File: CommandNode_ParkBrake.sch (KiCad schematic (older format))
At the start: 0 parts

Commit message: Created isolated RS585 interfaces and completed park brake.
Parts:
- added D? (x2): BAS16,215, RLOOP_FOOTPRINTS:rLoop_SOT23, symbol BAS16,215
- added P? (x2): TE_640456-8, RLOOP_FOOTPRINTS:rLoop_TE640456-8, symbol TE_640456-8
- added RL? (x2): TQ2-5V, RLOOP_FOOTPRINTS:rLoop_DIP10, symbol TQ2-5V
- added U? (x2): NUD3124LT1G, RLOOP_FOOTPRINTS:rLoop_SOT23, symbol NUD3124LT1G
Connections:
- net labels added: +24V_A, +5V_A, GNDD, PARK_BRAKE
- wire segments 0 -> 27
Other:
- note added: "Solenoids are 0.4A"
- note added: "rLoop - Command Node\nPark Brake Interface"

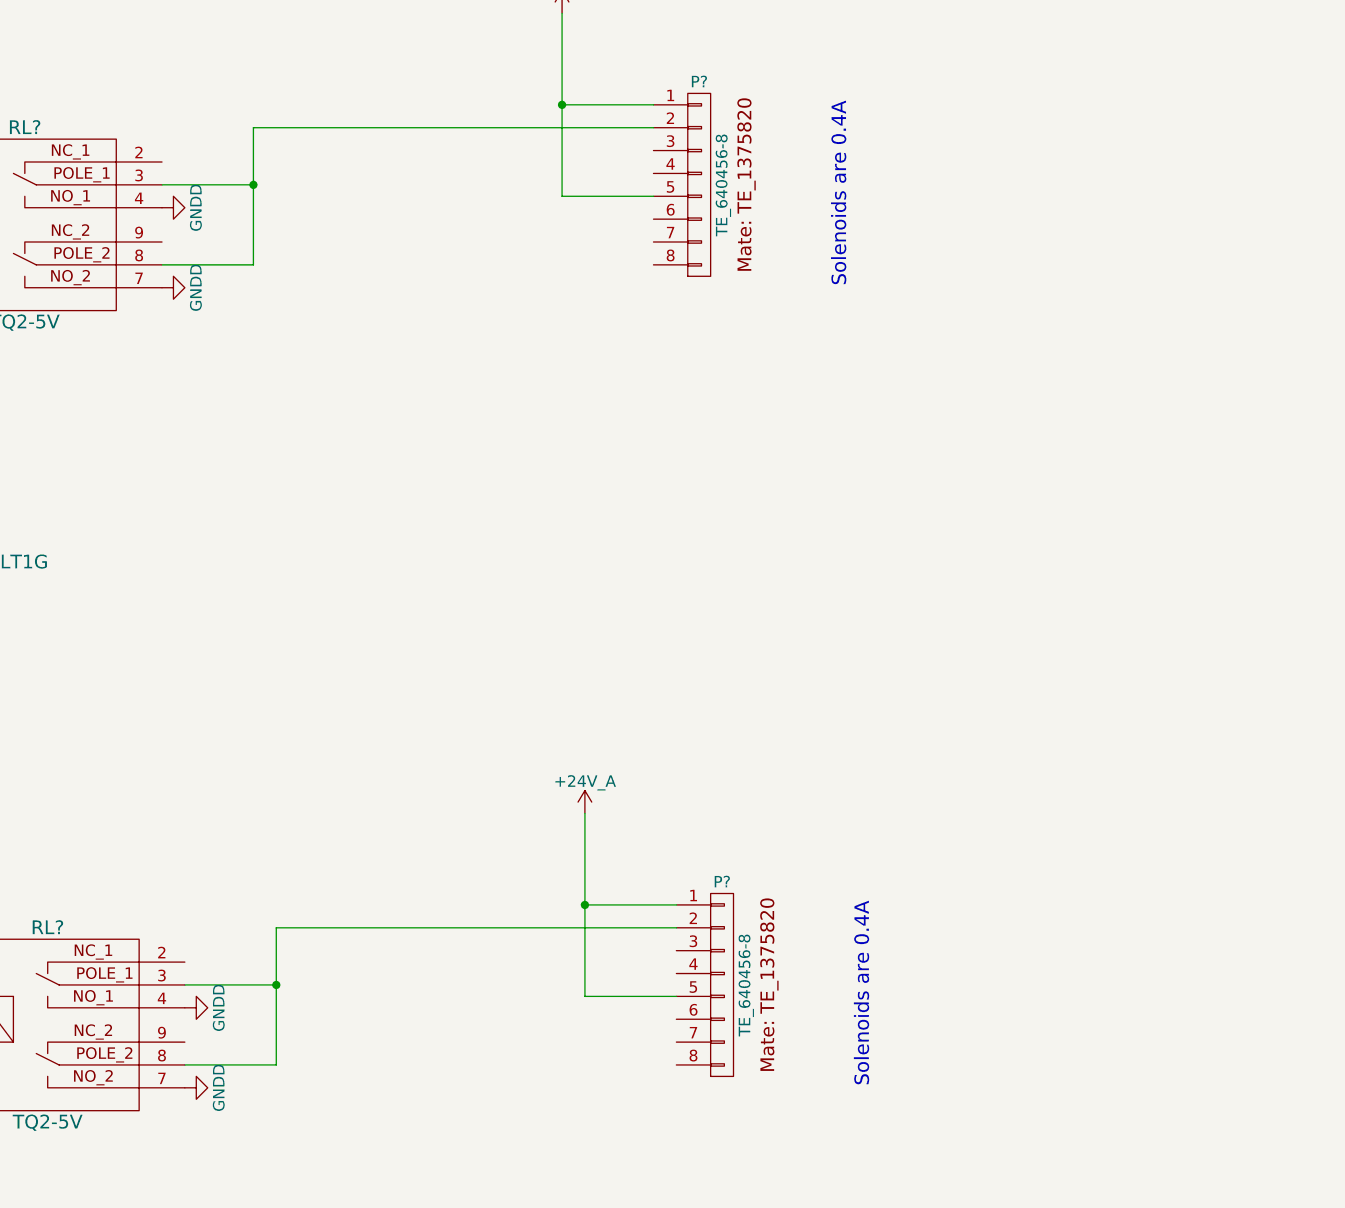
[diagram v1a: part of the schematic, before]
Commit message: Finish and print schematics for review
Lifting mechanism, charger interface, Data Enable on HE controller
RS585, Park Brake and node core.
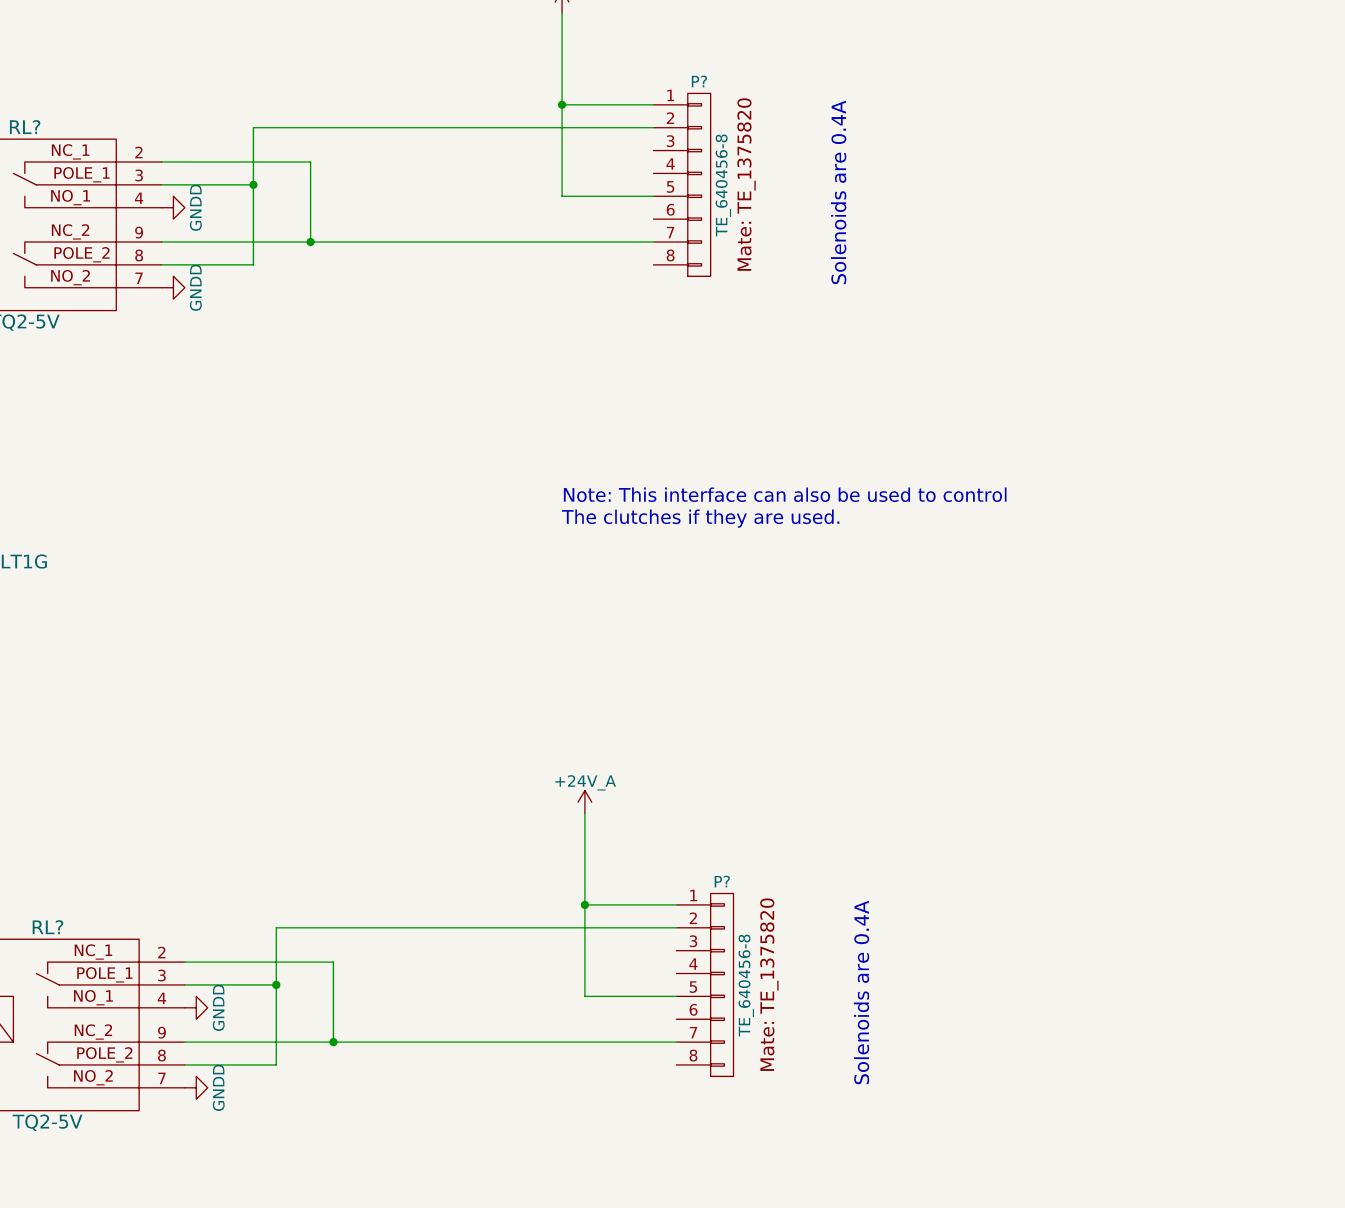
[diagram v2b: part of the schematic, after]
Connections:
- wire segments 27 -> 33
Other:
- note added: "Note: This interface can also be used to control \nThe clutches if they are used."
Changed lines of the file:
@@
 $Descr A3 16535 11693
 encoding utf-8
-Sheet 2 7
+Sheet 2 8
 Title "Park Brake Interface"
 Date ""
@@
 	5000 8650 5000 5150
 Connection ~ 5000 5150
+Text Notes 9550 5350 0    60   ~ 0
+Note: This interface can also be used to control \nThe clutches if they are used.
+Wire Wire Line
+	7800 4100 9950 4100
+Wire Wire Line
+	7800 3750 8450 3750
+Wire Wire Line
+	8450 3750 8450 4100
+Connection ~ 8450 4100
+Wire Wire Line
+	7900 7600 10050 7600
+Wire Wire Line
+	8550 7250 8550 7600
+Connection ~ 8550 7600
+Wire Wire Line
+	7900 7250 8550 7250
 $EndSCHEMATC
